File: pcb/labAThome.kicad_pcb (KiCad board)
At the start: 2 copper layers, 100 x 100 mm, 76 parts, among them J1 I2C, J10 SRV2, J11 3.5.24.GND, J12 NEOPIXEL, J13 Barrel_Jack_Switch, J14 Conn_Coaxial, J2 SRV1, J3 5V, J4 EXT, J5 VPS, J6 FAN3, J7 1wire, J8 1wire, J9 FAN1, K1 G5V-2, K2 G5V-2, K3 G5V-2, M1 HXJ8002_MODULE, M2 NEOPIXEL, M3 SN65HVD230_MODULE, Q1 IRLZ44N, Q2 IRLZ44N, Q3 IRLZ44N, Q5 2N3904, SW1 RED, SW2 GREEN, SW4 BLUE, SW5 WHITE, SW7 ROTENC, U1 SR602, U10 MAX3485_MODULE, U11 AM312, U2 24V->5V, U3 PDC004_Module, U4 ESP32_DEVKITC_COMPATIBLE, U5 LD06AJSA, U6 GY-302, U7 Display, U8 INMP441_Module, U9 RFM95W-868S2, X1 FAN_6024

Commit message: PCB labathomev5 as ordered at jlcpcb
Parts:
- removed M2: NEOPIXEL, smopla:NEOPIXEL_STICK
- removed Q5: 2N3904, Package_TO_SOT_THT:TO-92_HandSolder
- added C3: 1m, Capacitor_Tantalum_SMD:CP_EIA-7360-38_Kemet-E_Pad2.25x4.25mm_HandSolder, F.Cu at (66.3, 44.1)
- added FID1: OSHW, Symbol:OSHW-Logo_5.7x6mm_SilkScreen, B.Cu at (61.0, 100.3)
- added FID3: NonCommercial, Symbol:Symbol_CC-Noncommercial_CopperTop_Small, B.Cu at (61.0, 92.7)
- added GSM_Module1: SIM800L, smopla:SIM800L, F.Cu at (82.1, 45.3)
- added J15: WS2812_OUT, Connector_PinHeader_2.54mm:PinHeader_1x04_P2.54mm_Vertical, F.Cu at (112.6, 34.9)
- added Q4: BC847, Package_TO_SOT_SMD:SOT-23_Handsoldering, B.Cu at (103.2, 74.3)
- added U12: 24V->4V, sensact:MODULE_STEPDOWN, F.Cu at (57.4, 57.8)
- added m1: Attribution, Symbol:Symbol_CC-Attribution_CopperTop_Small, B.Cu at (61.0, 85.1)
- C1: footprint Capacitor_THT:CP_Radial_Tantal_D5.0mm_P5.00mm -> Capacitor_Tantalum_SMD:CP_EIA-3216-18_Kemet-A_Pad1.58x1.35mm_HandSolder
- C2: footprint Capacitor_THT:C_Rect_L4.0mm_W2.5mm_P2.50mm -> Capacitor_SMD:C_1206_3216Metric_Pad1.42x1.75mm_HandSolder
- D5: footprint Diode_THT:D_DO-41_SOD81_P7.62mm_Horizontal -> Diode_SMD:D_SMA_Handsoldering; moved to F.Cu
- D8: footprint Diode_THT:D_DO-35_SOD27_P2.54mm_Vertical_AnodeUp -> Diode_SMD:D_SMA_Handsoldering; moved to B.Cu
- J11: value 3.5.24.GND -> 24.5.GND.3
- J12: footprint Connector_PinSocket_2.54mm:PinSocket_1x04_P2.54mm_Vertical -> smopla:NEOPIXEL_STICK_alternativ
- J7, J8: footprint Connector_JST:JST_PH_B3B-PH-K_1x03_P2.00mm_Vertical -> Connector_JST:JST_XH_B3B-XH-A_1x03_P2.50mm_Vertical
- Q1, Q3: value IRLZ44N -> IRLML6344; footprint Package_TO_SOT_THT:TO-220-3_Horizontal_TabDown -> Package_TO_SOT_SMD:SOT-23_Handsoldering; moved to F.Cu
- R1, R12, R13, R14, R15, R16, R18, R19, R20, R21, R3, R5, R7: footprint Resistor_THT:R_Axial_DIN0207_L6.3mm_D2.5mm_P2.54mm_Vertical -> Resistor_SMD:R_1206_3216Metric_Pad1.42x1.75mm_HandSolder; moved to B.Cu
- R10: footprint Resistor_THT:R_Axial_DIN0207_L6.3mm_D2.5mm_P7.62mm_Horizontal -> Resistor_SMD:R_1206_3216Metric_Pad1.42x1.75mm_HandSolder
- R2, R4, R9: footprint Resistor_THT:R_Axial_DIN0207_L6.3mm_D2.5mm_P2.54mm_Vertical -> Resistor_SMD:R_1206_3216Metric_Pad1.42x1.75mm_HandSolder
- moved Q3 39.3 mm to (41.5, 65.5), turned to 180 degrees
- moved R4 30.9 mm to (44.2, 61.0), turned to 180 degrees
- moved J12 29.1 mm to (80.0, 38.7)
- moved Q1 27.4 mm to (41.5, 69.1), turned to 180 degrees
- moved R1 27.0 mm to (118.2, 59.9), turned to 0 degrees
- moved R3 20.8 mm to (51.2, 70.9), turned to 180 degrees
- moved C2 20.4 mm to (39.5, 91.3), turned to 270 degrees
- moved R12 19.2 mm to (102.4, 78.4), turned to 0 degrees
- moved R7 14.4 mm to (44.6, 87.8)
- moved R14 12.7 mm to (105.7, 101.6)
- moved D5 11.9 mm to (66.3, 55.5), turned to 270 degrees
- moved R21 11.6 mm to (39.5, 123.8), turned to 90 degrees
- moved R15 10.7 mm to (40.9, 106.7), turned to 180 degrees
- moved R19 10.4 mm to (40.5, 86.5)
- moved JP4 10.1 mm to (49.9, 67.8), turned to 180 degrees
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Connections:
- net Net-(JP6-Pad2) renamed SPI_MOSIx
- J11 pad 2: +5V -> GND
- J11 pad 3: +24V -> +5V
- J11 pad 4: GND -> +24V
- J4 pad 2: 485_DI -> 485_RO
- J4 pad 5: 485_RO -> 485_DI
- M3 pad 3: 485_DE -> 485_RO
- Q1 pad 2: /FAN_SWITCH2 -> GND
- Q1 pad 3: GND -> /FAN_SWITCH
- Q3 pad 2: /FAN_SWITCH -> GND
- Q3 pad 3: GND -> /FAN_SWITCH2
- R15 pad 2: Net-(Q3-Pad1) -> Net-(Q1-Pad1)
- R16 pad 2: Net-(Q3-Pad1) -> Net-(Q1-Pad1)
- R3 pad 2: Net-(Q1-Pad1) -> Net-(Q3-Pad1)
- R4 pad 2: Net-(Q1-Pad1) -> Net-(Q3-Pad1)
- U4 pad 26: 485_DI -> 485_RO
- U4 pad 27: 485_RO -> 485_DI
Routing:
- net Net-(Q1-Pad1): track 12.5 -> 64.1 mm, vias 0 -> 1
- net /FAN_SWITCH: track 48.8 -> 5.44 mm
- net /R3_INPUT: track 37.0 -> 4.48 mm, vias 1 -> 0
- net +4V: track 0.00 -> 27.6 mm
- net /FAN_SWITCH2: track 31.2 -> 4.51 mm
- net SPI_MISO: track 53.6 -> 76.2 mm, vias 0 -> 1
- net +24V: track 61.7 -> 83.1 mm
- net SPI_IO2: track 83.4 -> 103.4 mm
- net R3_A1: track 51.3 -> 71.2 mm
- net SPI_MOSIx: track 32.6 -> 51.8 mm, vias 0 -> 1
- net FAN2_DRIVE: track 3.81 -> 21.4 mm
- net 485_RO: track 54.4 -> 40.1 mm
- net Net-(D5-Pad1): track 38.4 -> 25.4 mm
- net ROTENC_A: track 30.4 -> 17.4 mm
- net Net-(D7-Pad2): track 14.0 -> 1.99 mm
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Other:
- board text added: "Für Lehre und Forschung Klaus Liebler, 2020-08-28 Westfälische Hochschule"
- board text added: "Gegenseitiger Ausschluss: - SERVO2,FAN1_SENSE - SERVO1,I2S,RS485,CAN,EXT"
- board text added: "LAB@HOME V5"
- board text removed: "Für Lehre und Forschung Klaus Liebler, 2020-08-11 Westfälische Hochschule"
- board text removed: "Gegenseitiger Ausschluss: - SERVO2 und FAN1_SENSE - I2S,RS485,CAN,EXT"
- board text removed: "LAB@HOME V4"

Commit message: Various big changes (sorry for beeing rude here...)
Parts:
- J14: footprint Connector_Coaxial:SMA_Amphenol_132289_EdgeMount -> Connector_Coaxial:SMA_Samtec_SMA-J-P-X-ST-EM1_EdgeMount
- J4: footprint Connector_JST:JST_XH_B5B-XH-AM_1x05_P2.50mm_Vertical -> Connector_JST:JST_XH_B6B-XH-A_1x06_P2.50mm_Vertical
- SPK1: moved to B.Cu
- moved JP5 20.0 mm to (82.3, 93.2)
- moved M1 10.5 mm to (91.6, 93.0)
- moved JP6 8.66 mm to (76.6, 76.3), turned to 0 degrees
- moved RV1 7.61 mm to (87.6, 101.0), turned to 180 degrees
- moved R2 6.61 mm to (103.7, 60.7), turned to 180 degrees
- moved JP8 6.01 mm to (77.0, 89.8)
- moved SPK1 5.70 mm to (91.4, 79.7)
- moved J1 3.95 mm to (86.7, 66.5)
- moved GSM_Module1 1.65 mm to (83.7, 45.3)
- moved U9 1.65 mm to (83.7, 44.3)
- moved C3 1.02 mm to (67.3, 43.9)
- moved JP9 0.89 mm to (77.0, 80.0)
- moved U5 0.63 mm to (49.9, 112.4)
- moved U7 0.51 mm to (82.7, 80.0)
- moved U4 0.38 mm to (66.9, 99.1)
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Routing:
- net GND: track 20.9 -> 41.4 mm, vias 386 -> 345
- net Net-(JP5-Pad2): track 39.6 -> 59.7 mm
- net SPI_CLK: track 28.7 -> 9.87 mm
- net SPI_IO2: track 103.4 -> 94.9 mm, vias 0 -> 1
- net SPI_MISO: track 76.2 -> 72.1 mm, vias 1 -> 0
- net +5V: track 282.4 -> 286.2 mm
- net Net-(JP8-Pad2): track 11.1 -> 13.8 mm
- net SCL: track 61.8 -> 64.4 mm
- net SPI_MOSI: track 7.85 -> 5.64 mm
- net R3_A1: track 71.2 -> 73.3 mm
- net SPI_MOSIx: track 51.8 -> 53.8 mm, vias 1 -> 2
- net Net-(M1-Pad1): track 11.6 -> 9.89 mm
- net 1wire: track 36.2 -> 34.6 mm
- net Net-(J14-Pad1): track 8.61 -> 7.05 mm
- net R3_ON: track 53.3 -> 51.9 mm
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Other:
- board text added: "LAB@HOME V6"
- board text removed: "LAB@HOME V5"

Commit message: labathome - first break through - simple and/or/rs working :-)
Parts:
- RV1: footprint Potentiometer_THT:Potentiometer_Runtron_RM-065_Vertical -> Potentiometer_THT:Potentiometer_Alps_RK09K_Single_Vertical
- SPK1: moved to F.Cu
- moved RV1 6.36 mm to (82.2, 104.2), turned to 0 degrees
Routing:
- net Net-(M1-Pad1): track 9.89 -> 16.9 mm
- net SPEAKER: track 31.8 -> 33.0 mm
- net R3_ON: track 51.9 -> 53.0 mm
- net GND: vias 345 -> 351

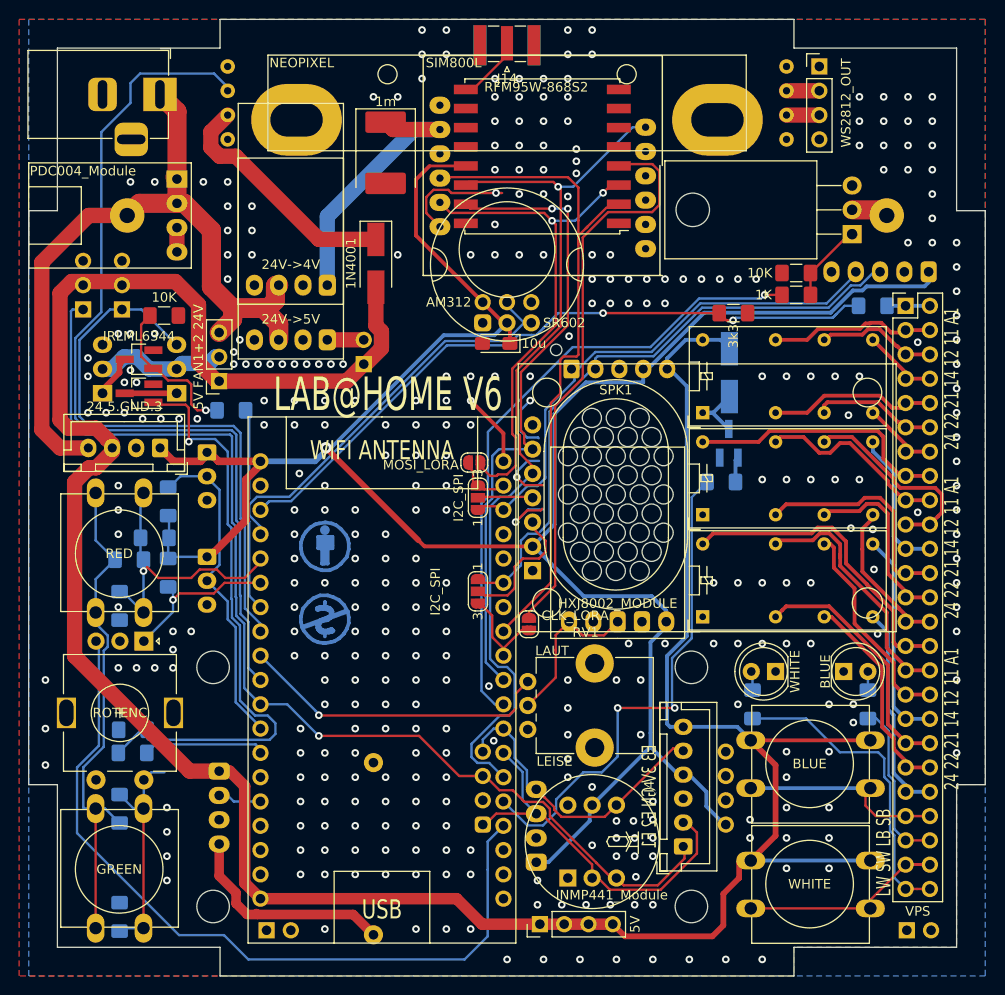
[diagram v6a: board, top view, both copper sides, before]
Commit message: Working experiment UI
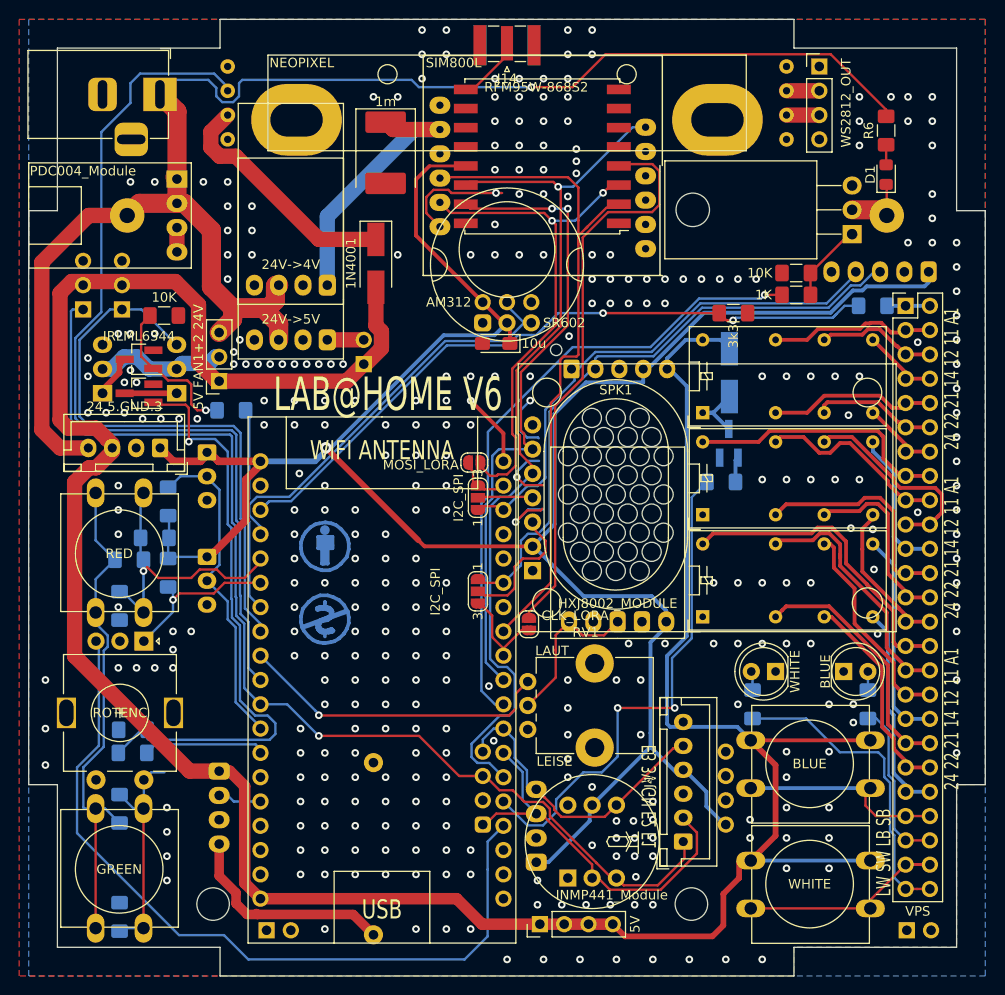
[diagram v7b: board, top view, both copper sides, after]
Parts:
- added D1: LED, LED_SMD:LED_0805_2012Metric_Pad1.15x1.40mm_HandSolder, F.Cu at (119.6, 46.2)
- added R6: 3K3, Resistor_SMD:R_1206_3216Metric_Pad1.42x1.75mm_HandSolder, F.Cu at (119.6, 41.6)
- moved J4 0.51 mm to (98.4, 116.0)
- moved X1 0.25 mm to (74.3, 110.0), turned to 0 degrees
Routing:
- net +24V: track 83.1 -> 167.7 mm, vias 0 -> 1
- net /Q2_D: track 3.87 -> 7.14 mm
- net Net-(D1-Pad2): track 0.00 -> 2.10 mm
- net GND: vias 351 -> 345

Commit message: Overall unspecific update
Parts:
- removed J10: SRV2, Connector_PinHeader_2.54mm:PinHeader_1x03_P2.54mm_Vertical
- removed J7: 1wire, Connector_JST:JST_XH_B3B-XH-A_1x03_P2.50mm_Vertical
- removed JP2, JP3: MECHANICAL, Connector_PinHeader_2.54mm:PinHeader_1x02_P2.54mm_Vertical
- removed R19: 4k7, Resistor_SMD:R_1206_3216Metric_Pad1.42x1.75mm_HandSolder
- added C4: u1, Capacitor_SMD:C_1206_3216Metric_Pad1.42x1.75mm_HandSolder, B.Cu at (45.5, 106.8)
- added C5: u1, Capacitor_SMD:C_1206_3216Metric_Pad1.42x1.75mm_HandSolder, B.Cu at (36.4, 100.1)
- added D10: 3528, LED_SMD:LED_PLCC_2835_Handsoldering, B.Cu at (35.2, 84.8)
- added D11: 3528, LED_SMD:LED_PLCC_2835_Handsoldering, B.Cu at (39.5, 90.7)
- added D2: 3528, LED_SMD:LED_PLCC_2835_Handsoldering, B.Cu at (39.5, 78.6)
- added D3: 3528, LED_SMD:LED_PLCC_2835_Handsoldering, B.Cu at (43.8, 84.8)
- added D9: 3528, LED_SMD:LED_PLCC_2835_Handsoldering, B.Cu at (39.5, 84.8)
- added Q5: IRLZ44N, Package_TO_SOT_THT:TO-220-3_Horizontal_TabDown, B.Cu at (56.6, 116.8)
- added R17: 1K, Resistor_SMD:R_1206_3216Metric_Pad1.42x1.75mm_HandSolder, B.Cu at (46.9, 111.9)
- added R22: K1, Resistor_SMD:R_1206_3216Metric_Pad1.42x1.75mm_HandSolder, B.Cu at (47.9, 104.9)
- added R23: 1k, Resistor_SMD:R_1206_3216Metric_Pad1.42x1.75mm_HandSolder, B.Cu at (50.3, 104.9)
- added R24: R1, Resistor_SMD:R_1206_3216Metric_Pad1.42x1.75mm_HandSolder, B.Cu at (61.3, 105.2)
- added R8: 1K, Resistor_SMD:R_1206_3216Metric_Pad1.42x1.75mm_HandSolder, B.Cu at (44.5, 111.9)
- added RV2: 10k, Potentiometer_SMD:Potentiometer_Vishay_TS53YL_Vertical, B.Cu at (42.4, 117.2)
- added U13: LM358, sensact:SOIC-8_3.9x4.9mm_Pitch1.27mm_handsolder, B.Cu at (39.4, 105.5)
- added j/1: 1wire, Connector_JST:JST_XH_B4B-XH-A_1x04_P2.50mm_Vertical, B.Cu at (48.9, 75.3)
- J2: value SRV1 -> SRVx; footprint Connector_PinHeader_2.54mm:PinHeader_1x03_P2.54mm_Vertical -> Connector_PinHeader_2.54mm:PinHeader_2x03_P2.54mm_Vertical
- J6: value FAN3 -> FAN2
- J8: footprint Connector_JST:JST_XH_B3B-XH-A_1x03_P2.50mm_Vertical -> Connector_JST:JST_XH_B4B-XH-A_1x04_P2.50mm_Vertical
- moved R5 20.6 mm to (49.4, 100.5), turned to 180 degrees
- moved C2 18.6 mm to (56.5, 83.7), turned to 90 degrees
- moved R16 18.1 mm to (58.9, 105.2), turned to 90 degrees
- moved R15 15.7 mm to (56.5, 105.2), turned to 90 degrees
- moved J8 13.5 mm to (48.9, 88.8)
- moved R7 12.0 mm to (56.5, 88.9), turned to 90 degrees
- moved R18 4.84 mm to (44.3, 79.5), turned to 270 degrees
- moved FID1 2.41 mm to (61.0, 97.9)
- moved R20 0.76 mm to (39.5, 111.8)
- moved J2 0.74 mm to (36.3, 59.9)
- moved C3 0.51 mm to (67.3, 44.5)
- moved R21 0.38 mm to (39.5, 123.4)
- moved R3 0.25 mm to (51.2, 70.6)
- moved GSM_Module1 0.09 mm to (83.6, 45.3)
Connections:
- net Net-(J6-Pad2) renamed /FAN_SUPPLY
- J2 pad 2: +5V -> FAN1_SENSE
- J2 pad 3: GND -> +5V
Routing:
- net Net-(D11-Pad1): track 0.00 -> 42.7 mm, vias 0 -> 1
- net +3V3: track 242.0 -> 262.3 mm, vias 1 -> 2
- net Net-(R19-Pad2): track 53.1 -> 73.1 mm
- net Net-(Q5-Pad3): track 0.00 -> 19.4 mm
- net Net-(Q1-Pad1): track 63.5 -> 46.1 mm
- net Net-(Q5-Pad1): track 0.00 -> 16.9 mm
- net LED_POWER_WHITE: track 4.07 -> 18.2 mm, vias 0 -> 1
- net Net-(R17-Pad1): track 0.00 -> 14.0 mm
- net Net-(C4-Pad2): track 0.00 -> 11.4 mm
- net FAN1_DRIVE: track 13.0 -> 2.32 mm
- net ROTENC_B: track 82.8 -> 92.5 mm
- net +24V: track 167.7 -> 175.6 mm
- net Net-(C4-Pad1): track 0.00 -> 6.92 mm
- net Net-(D2-Pad1): track 0.00 -> 5.83 mm
- net Net-(D10-Pad1): track 0.00 -> 5.67 mm
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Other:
- board text added: "LAB@HOME V5.1"
- board text added: "SRV1"
- board text added: "SRV2"
- board text removed: "LAB@HOME V6"
